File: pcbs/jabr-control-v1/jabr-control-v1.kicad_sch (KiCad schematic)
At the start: 4 parts

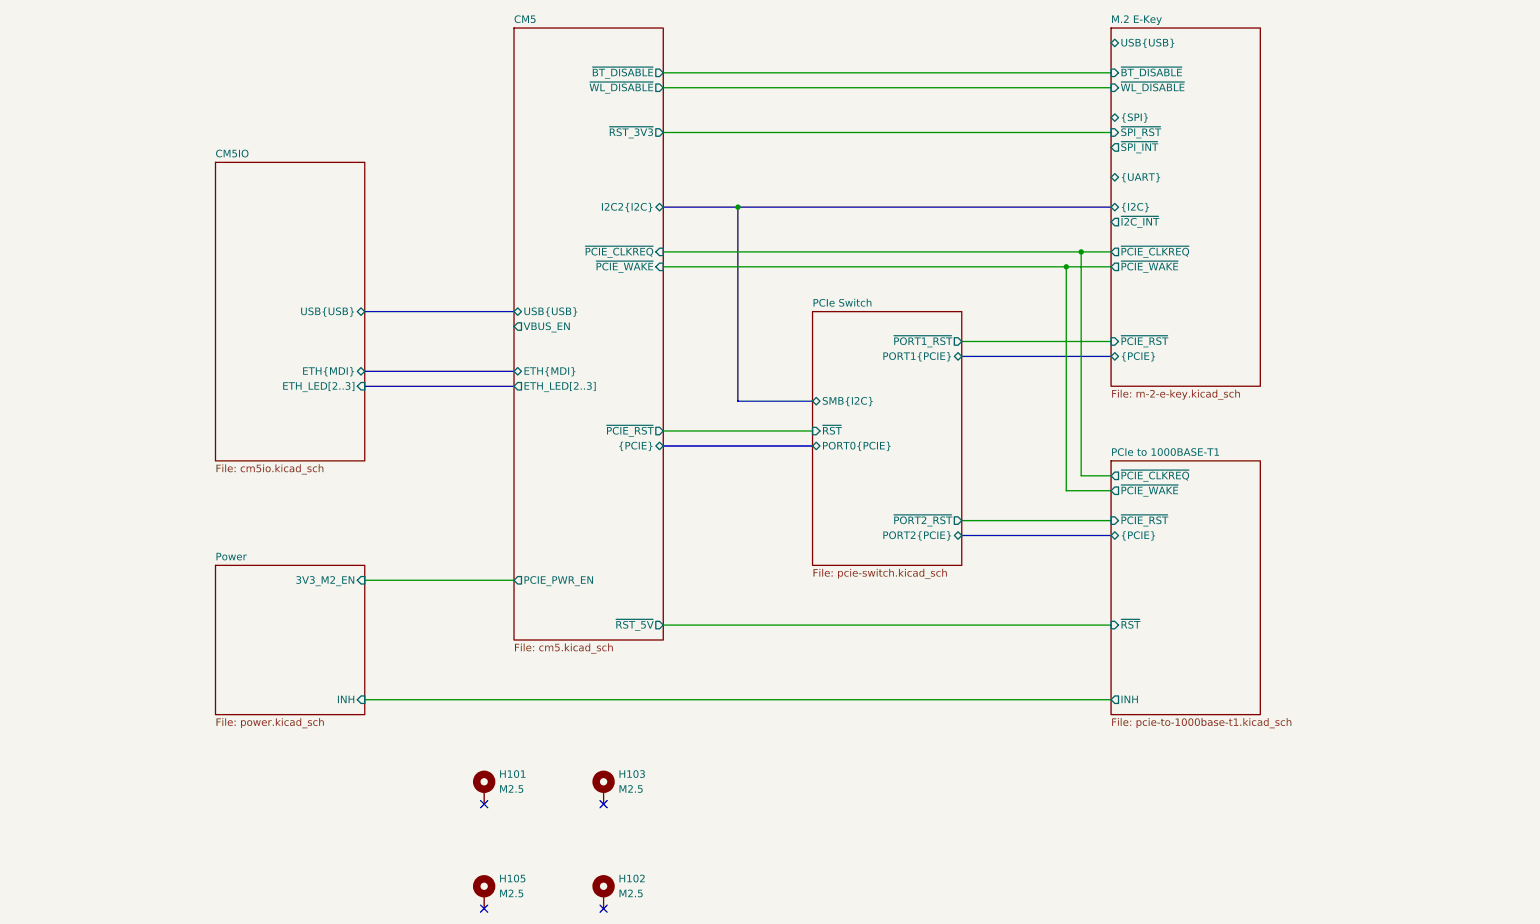
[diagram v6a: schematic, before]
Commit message: Schematic nearing completion, need to do GPIO and PHY decouplings caps
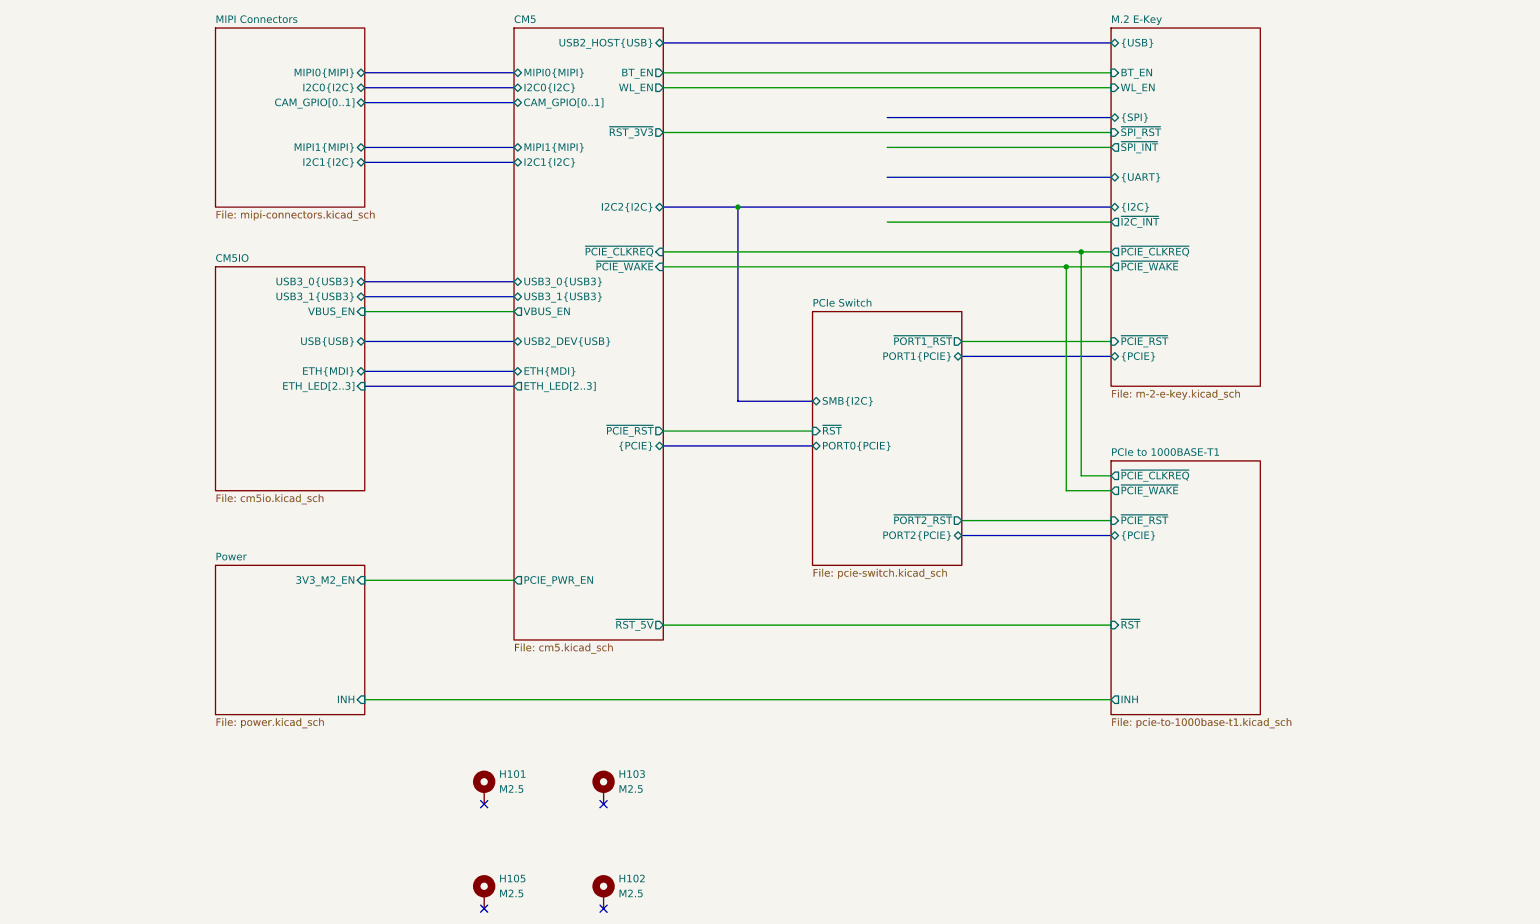
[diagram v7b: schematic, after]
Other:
- added sheet MIPI Connectors (mipi-connectors.kicad_sch)
- sheet CM5 ports: added BT_EN, CAM_GPIO[0..1], I2C0{I2C}, I2C1{I2C}, MIPI0{MIPI}, MIPI1{MIPI}, USB2_DEV{USB}, USB2_HOST{USB}, USB3_0{USB3}, USB3_1{USB3}, WL_EN; removed USB{USB}, ~{BT_DISABLE}, ~{WL_DISABLE}
- sheet CM5IO ports: added USB3_0{USB3}, USB3_1{USB3}, VBUS_EN; removed none
- sheet M.2 E-Key ports: added BT_EN, WL_EN, {USB}; removed USB{USB}, ~{BT_DISABLE}, ~{WL_DISABLE}
